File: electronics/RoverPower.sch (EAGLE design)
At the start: 13 parts, among them U1 LM2940

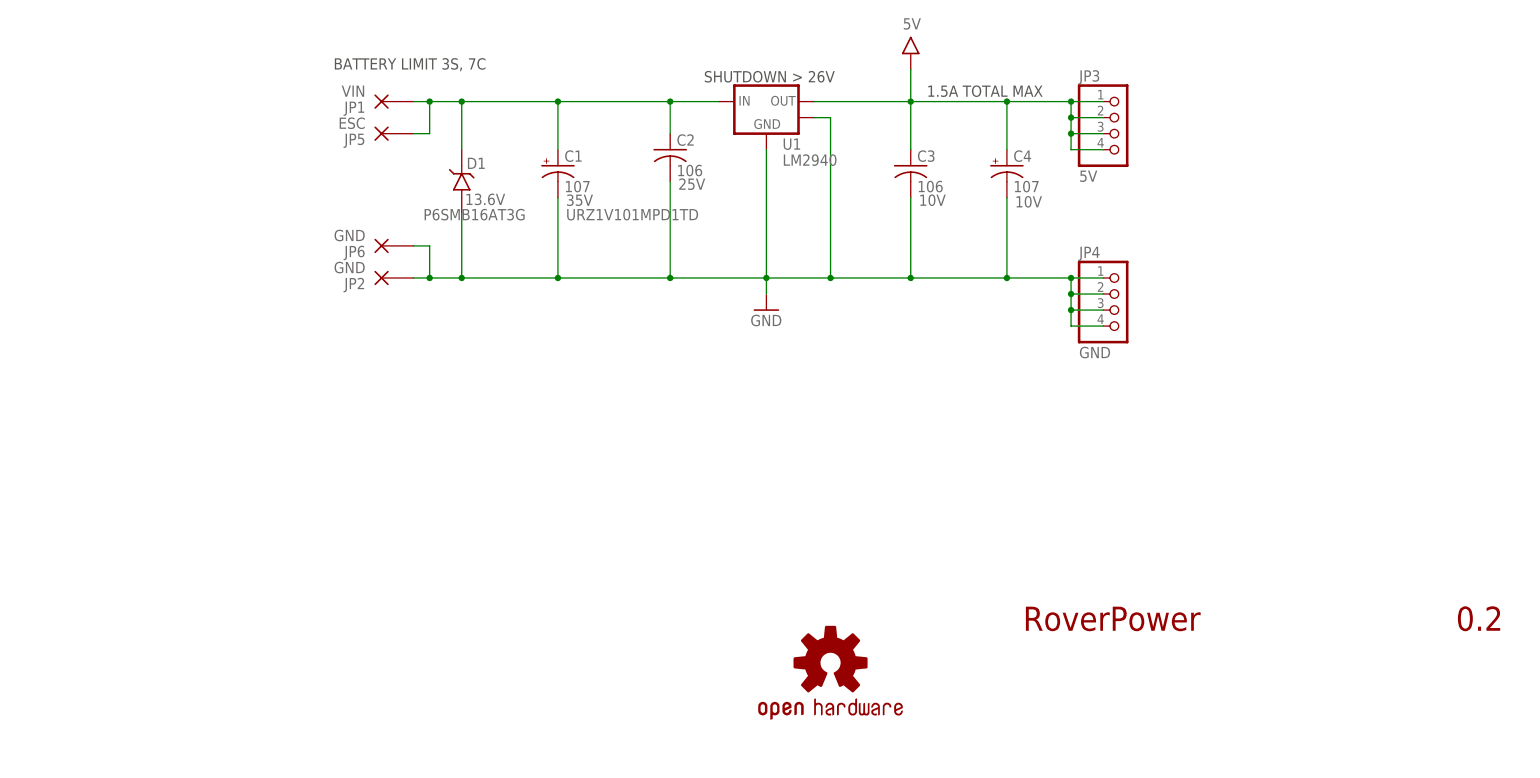
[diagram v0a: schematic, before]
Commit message: copied power polygons to bottom layer, added vias. Changed capacitor to smaller version, revised TVS to higher voltage, changed layout.
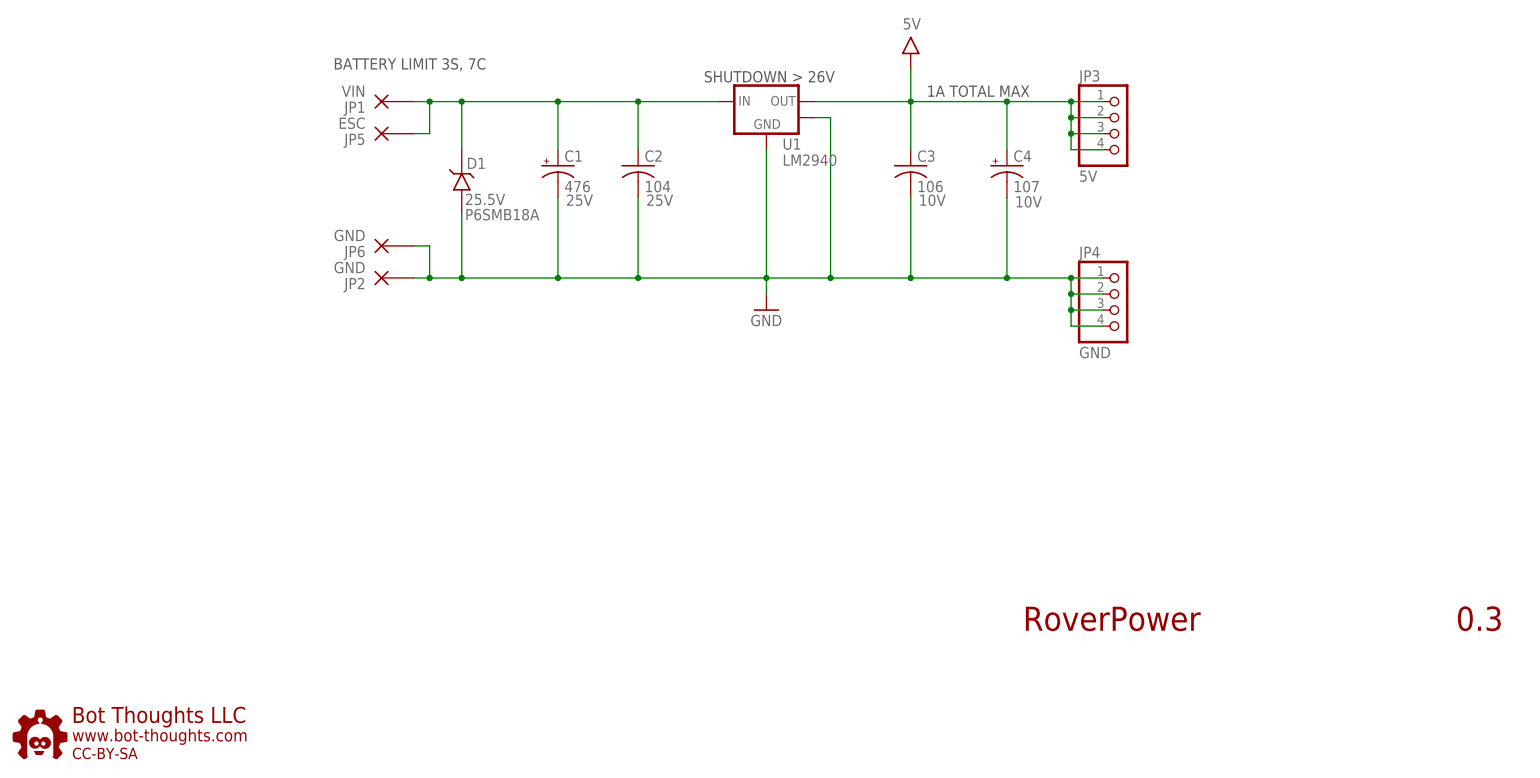
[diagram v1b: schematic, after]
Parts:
- removed LOGO1: OSHW-LOGOS, SparkFun-Aesthetics:OSHW-LOGOS
- added U$2: BTLOGO-LOGO-MD, bt:BTLOGO-LOGO-MD
- C1: value 107 -> 476; device rcl:CPOL-USE3.5-8 -> rcl:CPOL-USE2.5-6; PARTNO URZ1V101MPD1TD -> EEU-FC1H470; VOLTAGE 35V -> 25V
- C2: value 106 -> 104; device rcl:C-USC1206 -> rcl:C-USC0603
- D1: value 13.6V -> 25.5V; PARTNO P6SMB16AT3G -> P6SMB18A
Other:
- note added: "0.3"
- note added: "1A TOTAL MAX"
- note removed: "0.2"
- note removed: "1.5A TOTAL MAX"
- moved on the sheet: C2
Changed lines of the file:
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@@
 </classes>
 <parts>
-<part name="C2" library="rcl" deviceset="C-US" device="C1206" value="106">
-<attribute name="VOLTAGE" value="25V"/>
-</part>
 <part name="C3" library="rcl" deviceset="C-US" device="C1206" value="106">
 <attribute name="VOLTAGE" value="10V"/>
@@
 <part name="JP4" library="pinhead-2" deviceset="PINHD-1X04" device="_2.54-S" value="GND"/>
 <part name="FRAME1" library="bt" deviceset="LETTER_L" device=""/>
-<part name="C1" library="rcl" deviceset="CPOL-US" device="E3.5-8" value="107">
-<attribute name="PARTNO" value="URZ1V101MPD1TD"/>
-<attribute name="VOLTAGE" value="35V"/>
-</part>
-<part name="D1" library="bt_diode" deviceset="P6SMBXXAT3G" device="SMA" value="13.6V">
-<attribute name="PARTNO" value="P6SMB16AT3G"/>
+<part name="D1" library="bt_diode" deviceset="P6SMBXXAT3G" device="SMA" value="25.5V">
+<attribute name="PARTNO" value="P6SMB18A"/>
 </part>
 <part name="U1" library="bt_regulator" deviceset="LM2940" device="KTT" value="LM2940"/>
@@
 <part name="JP5" library="bt_electromech" deviceset="WIREPAD" device="_12GA" value="ESC"/>
 <part name="JP6" library="bt_electromech" deviceset="WIREPAD" device="_12GA" value="GND"/>
-<part name="LOGO1" library="SparkFun-Aesthetics" deviceset="OSHW-LOGO" device="S" value="OSHW-LOGOS"/>
+<part name="U$2" library="bt" deviceset="BTLOGO" device="-LOGO-MD"/>
+<part name="C1" library="rcl" deviceset="CPOL-US" device="E2.5-6" value="476">
+<attribute name="PARTNO" value="EEU-FC1H470"/>
+<attribute name="VOLTAGE" value="25V"/>
+</part>
+<part name="C2" library="rcl" deviceset="C-US" device="C0603" value="104">
+<attribute name="VOLTAGE" value="25V"/>
+</part>
 </parts>
 <sheets>
@@
 <plain>
 <text x="162.56" y="22.86" size="3.81" layer="94">RoverPower</text>
-<text x="231.14" y="22.86" size="3.81" layer="94">0.2</text>
-<text x="147.32" y="107.442" size="1.778" layer="97">1.5A TOTAL MAX</text>
+<text x="231.14" y="22.86" size="3.81" layer="94">0.3</text>
+<text x="147.32" y="107.442" size="1.778" layer="97">1A TOTAL MAX</text>
 <text x="53.34" y="111.76" size="1.778" layer="97">BATTERY LIMIT 3S, 7C</text>
 <text x="112.014" y="109.728" size="1.778" layer="97">SHUTDOWN &gt; 26V</text>
 </plain>
 <instances>
-<instance part="C2" gate="G$1" x="106.68" y="99.06">
-<attribute name="VOLTAGE" x="107.95" y="92.71" size="1.778" layer="96"/>
-</instance>
 <instance part="C3" gate="G$1" x="144.78" y="96.52">
 <attribute name="VOLTAGE" x="146.05" y="90.17" size="1.778" layer="96"/>
@@
 <instance part="FRAME1" gate="G$1" x="0" y="0"/>
 <instance part="FRAME1" gate="G$2" x="147.32" y="2.54"/>
-<instance part="C1" gate="G$1" x="88.9" y="96.52">
-<attribute name="VOLTAGE" x="90.17" y="90.17" size="1.778" layer="96"/>
-<attribute name="PARTNO" x="90.17" y="87.884" size="1.778" layer="96"/>
-</instance>
 <instance part="D1" gate="G$1" x="73.66" y="93.98" smashed="yes" rot="R90">
-<attribute name="PARTNO" x="67.564" y="87.884" size="1.778" layer="96"/>
+<attribute name="PARTNO" x="74.168" y="87.884" size="1.778" layer="96"/>
 <attribute name="NAME" x="74.422" y="96.012" size="1.778" layer="95"/>
 <attribute name="VALUE" x="74.168" y="90.297" size="1.778" layer="96"/>
@@
 <instance part="JP5" gate="G$1" x="60.96" y="101.6" rot="R180"/>
 <instance part="JP6" gate="G$1" x="60.96" y="83.82" rot="R180"/>
-<instance part="LOGO1" gate="G$1" x="132.08" y="17.78"/>
+<instance part="U$2" gate="G$1" x="2.54" y="2.54"/>
+<instance part="C1" gate="G$1" x="88.9" y="96.52">
+<attribute name="VOLTAGE" x="90.17" y="90.17" size="1.778" layer="96"/>
+</instance>
+<instance part="C2" gate="G$1" x="101.6" y="96.52">
+<attribute name="VOLTAGE" x="102.87" y="90.17" size="1.778" layer="96"/>
+</instance>
 </instances>
 <busses>
@@
 <wire x1="121.92" y1="78.74" x2="121.92" y2="76.2" width="0.1524" layer="91"/>
 <junction x="121.92" y="78.74"/>
-<pinref part="C2" gate="G$1" pin="2"/>
-<wire x1="106.68" y1="93.98" x2="106.68" y2="78.74" width="0.1524" layer="91"/>
-<wire x1="106.68" y1="78.74" x2="121.92" y2="78.74" width="0.1524" layer="91"/>
 <pinref part="JP2" gate="G$1" pin="P"/>
-<junction x="106.68" y="78.74"/>
-<wire x1="106.68" y1="78.74" x2="88.9" y2="78.74" width="0.1524" layer="91"/>
+<wire x1="121.92" y1="78.74" x2="101.6" y2="78.74" width="0.1524" layer="91"/>
 <pinref part="U1" gate="G$1" pin="GND"/>
 <pinref part="U1" gate="G$1" pin="TAB"/>
+<wire x1="101.6" y1="78.74" x2="88.9" y2="78.74" width="0.1524" layer="91"/>
 <wire x1="88.9" y1="78.74" x2="73.66" y2="78.74" width="0.1524" layer="91"/>
 <wire x1="73.66" y1="78.74" x2="68.58" y2="78.74" width="0.1524" layer="91"/>
@@
 <wire x1="132.08" y1="104.14" x2="132.08" y2="78.74" width="0.1524" layer="91"/>
 <junction x="132.08" y="78.74"/>
-<pinref part="C1" gate="G$1" pin="-"/>
 <wire x1="88.9" y1="91.44" x2="88.9" y2="78.74" width="0.1524" layer="91"/>
 <junction x="88.9" y="78.74"/>
@@
 <wire x1="68.58" y1="83.82" x2="68.58" y2="78.74" width="0.1524" layer="91"/>
 <junction x="68.58" y="78.74"/>
+<pinref part="C1" gate="G$1" pin="-"/>
+<pinref part="C2" gate="G$1" pin="2"/>
+<wire x1="101.6" y1="91.44" x2="101.6" y2="78.74" width="0.1524" layer="91"/>
+<junction x="101.6" y="78.74"/>
 </segment>
 </net>
 <net name="BAT+" class="0">
 <segment>
-<pinref part="C2" gate="G$1" pin="1"/>
-<wire x1="114.3" y1="106.68" x2="106.68" y2="106.68" width="0.1524" layer="91"/>
-<wire x1="106.68" y1="106.68" x2="106.68" y2="101.6" width="0.1524" layer="91"/>
-<wire x1="106.68" y1="106.68" x2="88.9" y2="106.68" width="0.1524" layer="91"/>
-<junction x="106.68" y="106.68"/>
 <pinref part="JP1" gate="G$1" pin="P"/>
 <pinref part="U1" gate="G$1" pin="VIN"/>
-<pinref part="C1" gate="G$1" pin="+"/>
+<wire x1="114.3" y1="106.68" x2="101.6" y2="106.68" width="0.1524" layer="91"/>
+<wire x1="101.6" y1="106.68" x2="88.9" y2="106.68" width="0.1524" layer="91"/>
 <wire x1="88.9" y1="106.68" x2="73.66" y2="106.68" width="0.1524" layer="91"/>
 <wire x1="73.66" y1="106.68" x2="68.58" y2="106.68" width="0.1524" layer="91"/>
@@
 <wire x1="68.58" y1="101.6" x2="68.58" y2="106.68" width="0.1524" layer="91"/>
 <junction x="68.58" y="106.68"/>
+<pinref part="C1" gate="G$1" pin="+"/>
+<pinref part="C2" gate="G$1" pin="1"/>
+<wire x1="101.6" y1="99.06" x2="101.6" y2="106.68" width="0.1524" layer="91"/>
+<junction x="101.6" y="106.68"/>
 </segment>
 </net>

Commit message: Added more vias, changed output 10uf to .1uf
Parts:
- C3: value 106 -> 104; device rcl:C-USC1206 -> rcl:C-USC0603
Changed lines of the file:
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@@
 </classes>
 <parts>
-<part name="C3" library="rcl" deviceset="C-US" device="C1206" value="106">
+<part name="C3" library="rcl" deviceset="C-US" device="C0603" value="104">
 <attribute name="VOLTAGE" value="10V"/>
 </part>
